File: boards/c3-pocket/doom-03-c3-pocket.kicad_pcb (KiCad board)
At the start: 2 copper layers, 52 x 92 mm, 40 parts, among them J2 S2B-PH-K-S(LF)(SN), Q1 FS8205A, SW9 JS102011SAQN, U1 ESP32-C3-MINI-1-N4X, U2 MCP73831T-2ACI/OT, U3 DW01A, U4 AP2112K-3.3TRG1, U5 ESD 2-line

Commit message: PCBKit's mark and pcbkit.io on every board; the RP2350 handheld ready to order
The handheld runs from two 18650 cells in parallel behind a DW01A protector and a reverse-cell
P-MOSFET, charged at up to 500 mA from the Pico's USB-C by a BQ24075 (power path into VSYS, timers
off for 6 Ah), with an on/off switch on 3V3_EN, M3 holes, ground pours and the console on pads.
Every assembled part has a JLCPCB code in stock (Basic where there is one); the module sockets are
in the BOM, the modules listed in the order's README. Check complete, the ready review clean.
Every board: routed and checked complete with the new mark.
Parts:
- added logo: , Logo_PCBKit_pcbkit.io, F.Cu at (106.8, 135.8)
- SW1, SW2, SW3, SW4, SW5, SW6, SW7, SW8: value (none) -> TS-1187A-B-A-B
- SW10: value (none) -> PTS645SM43SMTR92 LFS
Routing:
- net DN: track 80.2 -> 81.1 mm
- net DP: track 83.5 -> 84.3 mm

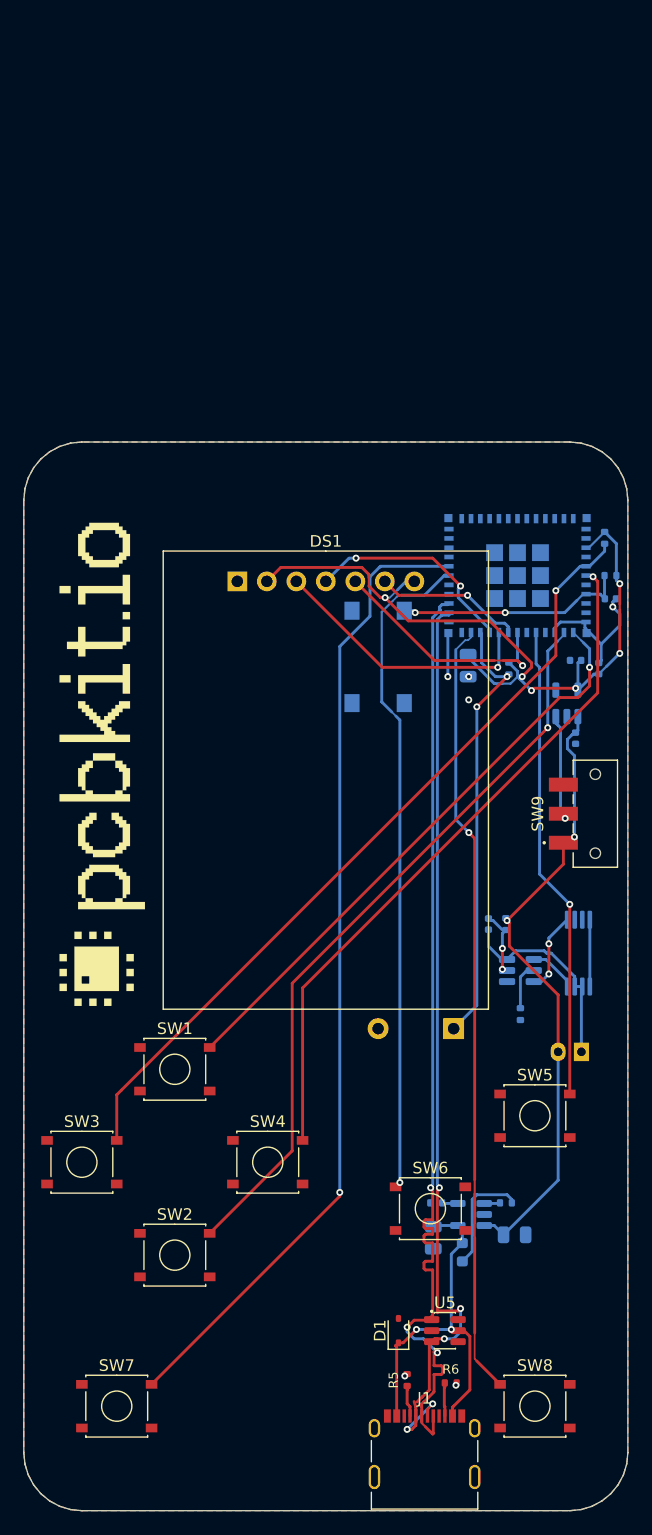
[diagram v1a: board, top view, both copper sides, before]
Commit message: c3-pocket: two 18650 cells with protection and a USB-C charger with power path; every part orderable
The LiPo on a JST plug with an MCP73831 becomes two 18650 upright on the back (Keystone 1042)
behind a reverse-cell P-FET and DW01A + FS8205A protection, a BQ24075 with power path from the
USB-C port (750 mA PTC, TVS, USBLC6-2 on the pair) feeding the AP2112K LDO, whose enable the slide
switch drives. Board 52 x 128 mm; USB-C at the left edge near the module (shorter pair), the
ESP32-C3-MINI-1-H4 (the -N4 is out of stock), M3 holes, test pads; every assembled part pinned to
an LCSC code; the README says how to charge and flash (USB Serial/JTAG, BOOT = MENU, RESET on the back).
check: complete, 0 errors, 3 warnings justified in the README (USB full-speed pair uncoupled and
skew, a GND stub narrowed); ready lens: nothing to fix; fab export without --force.

Claude-Session: https://claude.ai/code/session_01ATmMmxyrWxFwR3nTdXUrcx
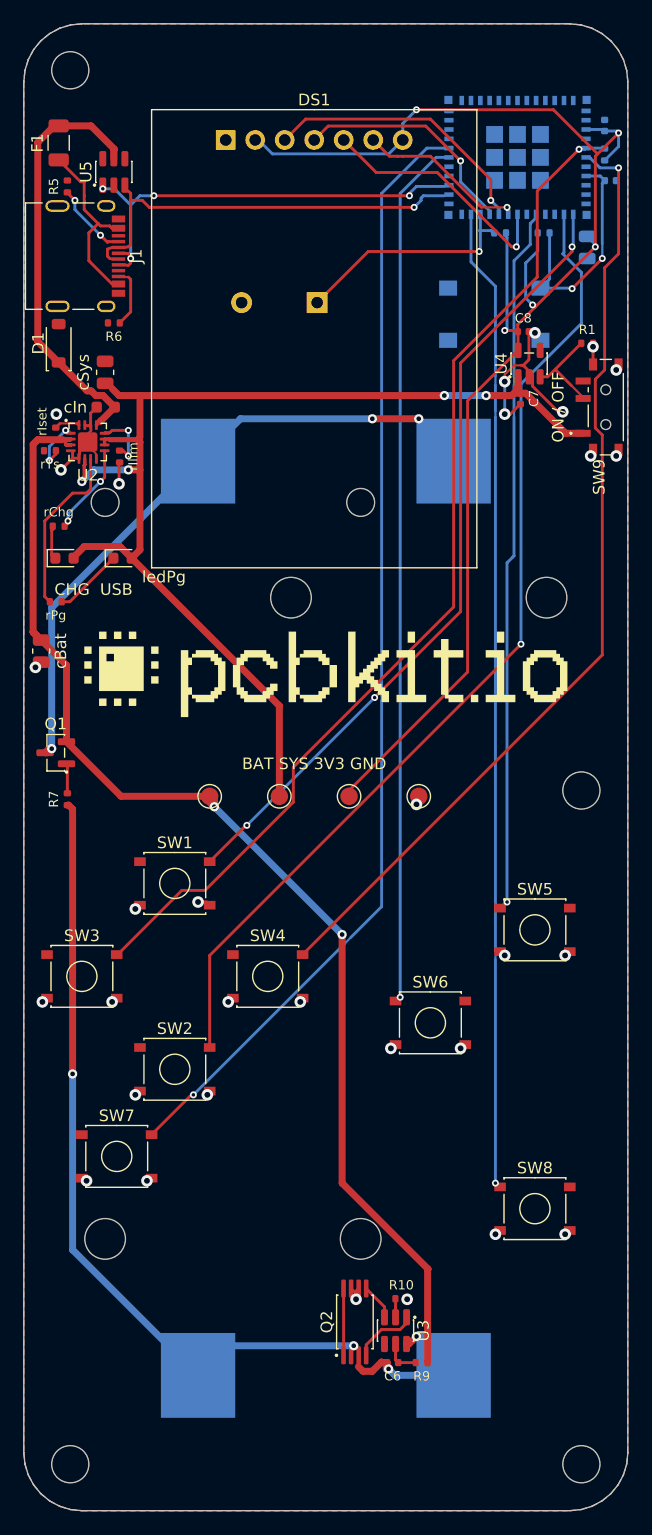
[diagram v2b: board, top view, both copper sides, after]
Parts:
- removed C4, C5: 4.7uF, C_0805_2012Metric
- removed D2: red, LED_0603_1608Metric
- removed J2: S2B-PH-K-S(LF)(SN), JST_PH_S2B-PH-K_1x02_P2.00mm_Horizontal
- removed R8: 470ohm, R_0402_1005Metric
- added BT1: 1042, BatteryHolder_Keystone_1042_1x18650, B.Cu at (115.0, 149.0)
- added BT2: 1042, BatteryHolder_Keystone_1042_1x18650, B.Cu at (137.0, 149.0)
- added F1: PTC 680mA, Fuse_1206_3216Metric, F.Cu at (103.0, 82.2)
- added H1: , MountingHole_3.2mm_M3, F.Cu at (104.0, 196.0)
- added H2: , MountingHole_3.2mm_M3, F.Cu at (148.0, 196.0)
- added H3: , MountingHole_3.2mm_M3, F.Cu at (104.0, 76.0)
- added H4: , MountingHole_3.2mm_M3, F.Cu at (148.0, 138.0)
- added Q2: FS8205A, TSSOP-8_4.4x2.93mm_P0.65mm, F.Cu at (128.5, 183.8)
- added cBat: 4.7uF, C_0805_2012Metric, F.Cu at (101.5, 126.0)
- added cIn: 1uF, C_0603_1608Metric, F.Cu at (107.0, 105.0)
- added cSys: 4.7uF, C_0805_2012Metric, F.Cu at (107.0, 102.0)
- added ledChg: red, LED_0603_1608Metric, F.Cu at (103.5, 118.0)
- added ledPg: green, LED_0603_1608Metric, F.Cu at (108.5, 118.0)
- added rChg: 1.5kohm, R_0402_1005Metric, F.Cu at (103.0, 115.2)
- added rIlim: 1.18kohm, R_0402_1005Metric, F.Cu at (108.2, 109.2)
- added rIset: 1.13kohm, R_0402_1005Metric, F.Cu at (102.8, 106.2)
- added rPg: 1.5kohm, R_0402_1005Metric, F.Cu at (102.8, 121.8)
- added rTs: 10kohm, R_0402_1005Metric, F.Cu at (102.2, 108.8)
- added tpBat: , TestPoint_Round_D1.5mm, F.Cu at (116.0, 138.5)
- added tpGnd: , TestPoint_Round_D1.5mm, F.Cu at (134.0, 138.5)
- added tpSys: , TestPoint_Round_D1.5mm, F.Cu at (122.0, 138.5)
- added tpV3: , TestPoint_Round_D1.5mm, F.Cu at (128.0, 138.5)
- C6, C7, C8, R10, R9, U3, U4: moved to F.Cu
- D1: footprint D_SOD-323 -> D_SOD-123
- Q1: value FS8205A -> AO3401A; footprint TSSOP-8_4.4x2.93mm_P0.65mm -> SOT-23; moved to F.Cu
- R1: value 100kohm -> 1Mohm; moved to F.Cu
- R7: value 2kohm -> 100kohm; moved to F.Cu
- SW9: value JS102011SAQN -> MSK12C02; footprint SW_Slide_SPDT_CK_JS102011SAQN_Horizontal -> SW_Slide_SPDT_Shouhan_MSK12C02
- U1: value ESP32-C3-MINI-1-N4X -> ESP32-C3-MINI-1-H4
- U2: value MCP73831T-2ACI/OT -> BQ24075RGTR; footprint SOT-23-5 -> QFN-16-1EP_3x3mm_P0.5mm_EP1.68x1.68mm; moved to F.Cu
- moved R5 106.8 mm to (103.8, 86.0)
- moved U5 103.7 mm to (107.8, 84.8), turned to 90 degrees
- moved J1 103.3 mm to (108.2, 92.0), turned to 270 degrees
- moved R6 95.7 mm to (107.8, 97.8), turned to 180 degrees
- moved D1 89.9 mm to (103.0, 99.5)
- moved U2 74.2 mm to (105.5, 108.0)
- moved BZ1 63.6 mm to (122.0, 96.0)
- moved Q1 48.2 mm to (102.8, 134.8), turned to 180 degrees
- moved R7 47.1 mm to (103.8, 138.8), turned to 90 degrees
- moved C2 46.1 mm to (150.0, 80.8), turned to 270 degrees
- moved R1 40.6 mm to (148.5, 99.5)
- moved C6 38.6 mm to (131.8, 187.2), turned to 180 degrees
- moved R9 38.4 mm to (134.2, 187.2), turned to 180 degrees
- moved DS1 38.0 mm to (125.0, 82.0)
- moved R4 37.5 mm to (141.0, 90.0), turned to 180 degrees
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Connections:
- C6 pad 2: BAT_N -> CELL_N
- C7 pad 1: VBAT -> SYS
- J1 pad A4: VBUS -> usb/power/raw
- J1 pad B4: VBUS -> usb/power/raw
- Q1 pad 1: U3Support/DRAIN -> reversed/gate
- Q1 pad 2: BAT_N -> BAT
- Q1 pad 3: BAT_N -> BAT_IN
- R3 pad 1: LEFT -> V3
- R3 pad 2: V3 -> LEFT
- R4 pad 1: V3 -> BUZZ
- R4 pad 2: BUZZ -> V3
- R7 pad 1: Net-(R7-1) -> CELL_N
- R7 pad 2: GND -> reversed/gate
- R9 pad 1: Net-(C6-1) -> BAT
- R9 pad 2: VBAT -> Net-(C6-1)
- SW9 pad 1: VBAT -> SYS
- SW9 pad 3: GND -> (no net)
- U2 pad 1: Net-(R8-2) -> TS
- U2 pad 2: GND -> BAT
- U2 pad 3: VBAT -> BAT
- U2 pad 4: VBUS -> GND
- U2 pad 5: Net-(R7-1) -> GND
- U3 pad 1: Net-(Q1-4) -> Net-(Q2-4)
- U3 pad 3: Net-(Q1-5) -> Net-(Q2-5)
- U3 pad 6: BAT_N -> CELL_N
- U4 pad 1: VBAT -> SYS
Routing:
- net BAT: track 0.00 -> 115.3 mm, vias 0 -> 2
- net SYS: track 0.00 -> 101.0 mm, vias 0 -> 4
- net CELL_N: track 0.00 -> 79.6 mm, vias 0 -> 4
- net V3: track 65.8 -> 124.5 mm, vias 6 -> 5
- net VBAT: track 52.6 -> 0.00 mm, vias 2 -> 0
- net BAT_IN: track 0.00 -> 51.9 mm, vias 0 -> 3
- net DP: track 84.3 -> 37.1 mm, vias 3 -> 4
- net DN: track 81.1 -> 34.6 mm, vias 5 -> 1
- net RIGHT: track 59.9 -> 82.7 mm
- net DOWN: track 64.4 -> 85.7 mm
- net FIRE: track 40.9 -> 61.1 mm
- net LEFT: track 69.2 -> 89.3 mm
- net UP: track 50.8 -> 68.7 mm, vias 1 -> 3
- net USE: track 56.9 -> 74.7 mm
- net BAT_N: track 17.7 -> 0.00 mm
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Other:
- board size 52 x 92 mm -> 52 x 128 mm
- board text added: "+"
- board text added: "-"
- board text added: "2 x 18650 Li-ion 3.7 V"
- board text added: "BAT SYS 3V3 GND"
- board text added: "CHG USB"
- board text added: "ON / OFF"
